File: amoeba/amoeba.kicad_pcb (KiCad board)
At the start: 2 copper layers, 18.8 x 16.1 mm, 14 parts

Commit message: Cleaned up Amoeba PCB.
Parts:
- removed D1: DIODE, D3
- removed LC (x3), LR (x2), SC (x3), SR (x2): CONN_1, Pad
- removed LED1: LED, LED-3MM
- removed R1: RESISTOR, RESISTOR
- removed S1: MX1A, CHERRY_PCB_100H
- added D0: DIODE, D3, B.Cu at (248.9, 115.6)
- added L0: LED, LED-3MM, F.Cu at (248.9, 115.6)
- added LC0:0: CONN_1, Pad, F.Cu at (246.4, 105.4)
- added LC0:1: CONN_1, Pad, F.Cu at (242.6, 118.1)
- added LC0:2: CONN_1, Pad, F.Cu at (252.7, 118.1)
- added LR0:0: CONN_1, Pad, F.Cu at (242.6, 115.6)
- added LR0:1: CONN_1, Pad, F.Cu at (255.3, 115.6)
- added R0: RESISTOR, RESISTOR, B.Cu at (248.9, 113.0)
- added S0: MX1A, CHERRY_PCB_100H, F.Cu at (248.9, 110.5)
- added SC0:0: CONN_1, Pad, F.Cu at (248.9, 105.4)
- added SC0:1: CONN_1, Pad, F.Cu at (245.1, 118.1)
- added SC0:2: CONN_1, Pad, F.Cu at (255.3, 118.1)
- added SR0:0: CONN_1, Pad, F.Cu at (242.6, 106.7)
- added SR0:1: CONN_1, Pad, F.Cu at (255.3, 106.7)
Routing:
- net /key/LC0: track 0.00 -> 28.1 mm, vias 0 -> 2
- net /key/SC0: track 0.00 -> 25.7 mm
- net N-000006: track 28.1 -> 6.13 mm, vias 2 -> 1
- net /key/SR0: track 0.00 -> 21.5 mm, vias 0 -> 1
- net N-000001: track 21.4 -> 0.00 mm, vias 1 -> 0
- net N-000004: track 15.5 -> 0.00 mm
- net /key/LR0: track 0.00 -> 15.5 mm
- net N-000007: track 13.3 -> 0.00 mm, vias 1 -> 0
- net N-000005: track 25.7 -> 13.3 mm, vias 0 -> 1
- net N-000003: track 6.13 -> 0.00 mm, vias 1 -> 0

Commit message: Fixes for Oshpark submission and minor labeling adjustments.
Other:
- board text added: "MX"
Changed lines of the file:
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@@
     (area 239.191799 96.874 258.648201 120.218201)
     (thickness 1.6)
-    (drawings 77)
+    (drawings 78)
     (tracks 49)
     (zones 0)
@@
     (mod_text_size 1 1)
     (mod_text_width 0.15)
-    (pad_size 1.5 1.5)
-    (pad_drill 0.6)
+    (pad_size 0.3302 0.3302)
+    (pad_drill 0.3302)
     (pad_to_mask_clearance 0)
     (aux_axis_origin 0 0)
-    (visible_elements FFFFFB3F)
+    (visible_elements FFFFF33F)
     (pcbplotparams
       (layerselection 284196865)
@@
     )
   )
-  (gr_text O (at 253.365 108.5215) (layer B.SilkS)
-    (effects (font (size 1 1) (thickness 0.25) italic) (justify mirror))
-  )
-  (gr_text M (at 254.889 108.839) (layer B.SilkS)
-    (effects (font (size 1 1) (thickness 0.25) italic) (justify mirror))
-  )
-  (gr_text A (at 249.6185 107.5055) (layer B.SilkS)
-    (effects (font (size 1 1) (thickness 0.25) italic) (justify mirror))
-  )
-  (gr_text A (at 256.159 109.728) (layer B.SilkS)
-    (effects (font (size 1 1) (thickness 0.25) italic) (justify mirror))
-  )
-  (gr_text E (at 252.1585 109.093) (layer B.SilkS)
-    (effects (font (size 1 1) (thickness 0.25) italic) (justify mirror))
-  )
-  (gr_text B (at 250.952 108.331) (layer B.SilkS)
+  (gr_text MX (at 245.8974 109.8804) (layer B.SilkS)
+    (effects (font (size 0.6 0.6) (thickness 0.15) italic) (justify mirror))
+  )
+  (gr_text O (at 249.95124 107.6579) (layer B.SilkS)
+    (effects (font (size 1 1) (thickness 0.25) italic) (justify mirror))
+  )
+  (gr_text M (at 251.08916 108.13796) (layer B.SilkS)
+    (effects (font (size 1 1) (thickness 0.25) italic) (justify mirror))
+  )
+  (gr_text A (at 247.03532 107.8357) (layer B.SilkS)
+    (effects (font (size 1 1) (thickness 0.25) italic) (justify mirror))
+  )
+  (gr_text A (at 251.99594 108.77804) (layer B.SilkS)
+    (effects (font (size 1 1) (thickness 0.25) italic) (justify mirror))
+  )
+  (gr_text E (at 248.92 107.42676) (layer B.SilkS)
+    (effects (font (size 1 1) (thickness 0.25) italic) (justify mirror))
+  )
+  (gr_text B (at 247.92432 107.42676) (layer B.SilkS)
     (effects (font (size 1 1) (thickness 0.25) italic) (justify mirror))
   )
@@
   (gr_line (start 247.5865 117.7925) (end 245.11 117.7925) (angle 90) (layer B.SilkS) (width 0.2))
   (gr_line (start 249.2375 117.0305) (end 249.2375 118.364) (angle 90) (layer B.SilkS) (width 0.2))
-  (gr_line (start 248.3485 107.061) (end 248.3485 105.41) (angle 90) (layer B.SilkS) (width 0.1))
+  (gr_line (start 248.36628 105.51414) (end 248.36628 103.86314) (angle 90) (layer B.SilkS) (width 0.1))
   (gr_line (start 256.8575 117.475) (end 255.27 117.475) (angle 90) (layer B.SilkS) (width 0.2))
   (gr_line (start 241.046 117.475) (end 242.57 117.475) (angle 90) (layer B.SilkS) (width 0.2))
@@
     (effects (font (size 0.8 0.8) (thickness 0.2)) (justify left mirror))
   )
-  (gr_text SC (at 248.2215 106.807) (layer B.SilkS)
+  (gr_text SC (at 248.27992 104.26192) (layer B.SilkS)
     (effects (font (size 0.6 0.6) (thickness 0.15)) (justify left mirror))
   )

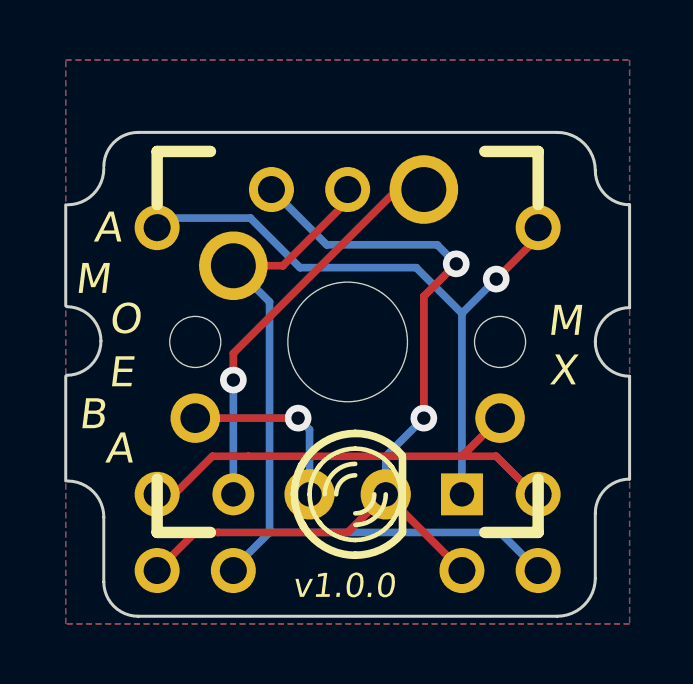
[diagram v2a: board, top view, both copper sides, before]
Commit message: Added surface mount pads to Amoeba and bumped version number to 1.1.0.
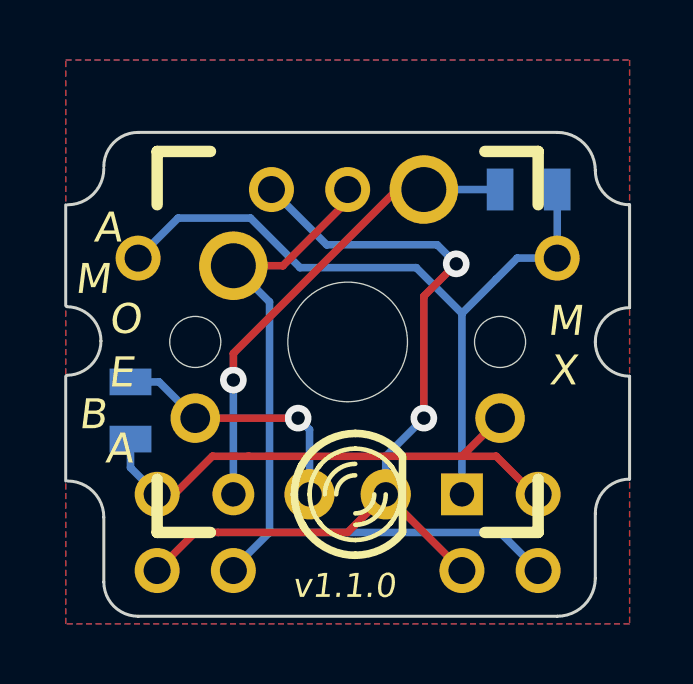
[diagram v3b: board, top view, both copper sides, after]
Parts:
- added D1: DIODE, SM0805D, B.Cu at (255.0, 105.4)
- added R1: RESISTOR, SM0805, B.Cu at (241.7, 112.8)
- moved SR0:0 1.20 mm to (241.9, 107.7)
- moved SR0:1 1.20 mm to (255.9, 107.7)
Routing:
- net /key/SR0: track 21.5 -> 24.9 mm, vias 1 -> 0
- net N-000005: track 6.13 -> 8.79 mm
- net N-000006: track 13.3 -> 15.9 mm
- net /key/LR0: track 15.5 -> 17.7 mm
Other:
- board text added: "v1.1.0"
- board text removed: "v1.0.0"
